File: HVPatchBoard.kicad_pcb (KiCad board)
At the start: 2 copper layers, 80 x 39.1 mm, 40 parts, among them J1 Conn_01x01_Male, J2 Conn_01x01_Male, J3 Conn_01x01_Male, J4 Conn_01x01_Male, J43 Conn_01x01_Male, J44 Conn_01x01_Male, J45 Conn_01x01_Male, J46 Conn_01x01_Male, J5 Conn_01x01_Male, J6 Conn_01x01_Male

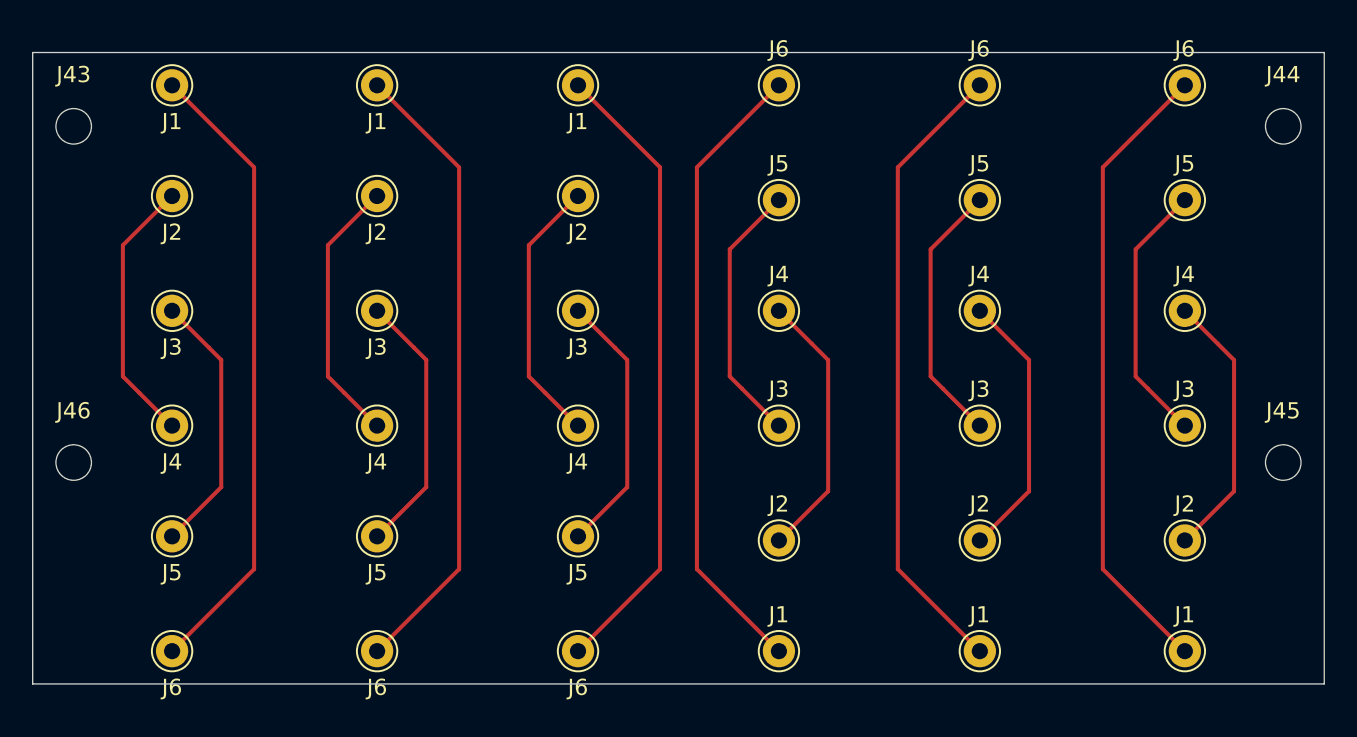
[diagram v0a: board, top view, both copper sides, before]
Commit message: Generated STEP file of patch board with individual grounds.
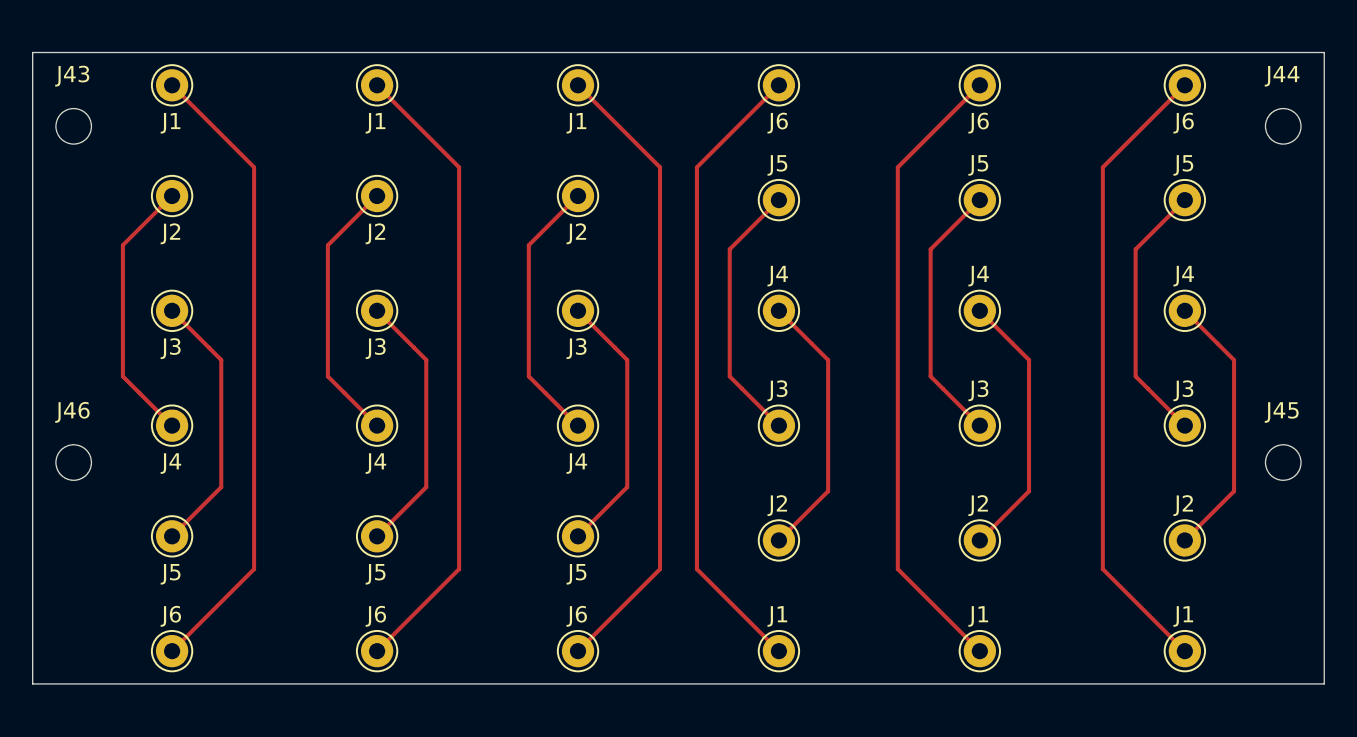
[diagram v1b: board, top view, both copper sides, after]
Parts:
- J1 (x6), J2 (x6), J3 (x6), J4 (x6), J5 (x6), J6 (x6): footprint Connector_Pin:Pin_D1.0mm_L10.0mm -> LEGENDHVLongConnector:HarwinPin
- turned J6 to 0 degrees (x3)
- turned J6 to 180 degrees (x3)
